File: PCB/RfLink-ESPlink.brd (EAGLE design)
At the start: 96 x 90 mm, 55 parts, among them IC1 WEMOS D1 MINI, IC2 ARDUINO-MEGA, IC3 PRO MINI 3.3V, IC4 CC2500 MODUL, IC5 TRANSMITTER 433MHZ, IC6 RXB6, IC7 RTX-MID, IC8 NRF24L01A, J2 JUMPER-3SMD, U1 AMS1117, U2 DHT22, U3 DS18B20, X1 BU-SMA-V

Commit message: Update Schema
Moved R5 closer to Mega 2560
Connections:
- net RX-TX renamed ESP-TX
- net TX-RX-L renamed ESP-RX
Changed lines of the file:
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@@
 <wire x1="93.599" y1="4.448725" x2="90.420275" y2="1.27" width="0.3048" layer="16"/>
 </signal>
-<signal name="RX-TX">
+<signal name="ESP-TX">
 <contactref element="IC1" pad="TX"/>
 <contactref element="IC3" pad="2"/>
@@
 </signal>
 <signal name="TX-RX">
+<contactref element="IC2" pad="1"/>
 <contactref element="R5" pad="2"/>
-<contactref element="IC2" pad="1"/>
-<wire x1="54.61" y1="43.18" x2="47.94" y2="43.18" width="0.3048" layer="1"/>
+<wire x1="47.94" y1="43.18" x2="54.61" y2="43.18" width="0.3048" layer="1"/>
 </signal>
-<signal name="TX-RX-L">
-<contactref element="R5" pad="1"/>
+<signal name="ESP-RX">
 <contactref element="IC1" pad="RX"/>
 <contactref element="IC3" pad="1"/>
@@
 <wire x1="43.18" y1="29.21" x2="43.18" y2="43.18" width="0.3048" layer="16"/>
 <via x="43.18" y="43.18" extent="1-16" drill="0.6"/>
-<wire x1="43.18" y1="43.18" x2="46.04" y2="43.18" width="0.3048" layer="1"/>
 <wire x1="56.1975" y1="82.2325" x2="58.42" y2="84.455" width="0.3048" layer="1"/>
 <wire x1="58.42" y1="84.455" x2="62.5475" y2="84.455" width="0.3048" layer="1"/>
@@
 <wire x1="55.41581875" y1="72.15430625" x2="53.686325" y2="73.8838" width="0.3048" layer="1"/>
 <wire x1="56.1975" y1="74.5188" x2="56.1975" y2="82.2325" width="0.3048" layer="1"/>
+<contactref element="R5" pad="1"/>
+<wire x1="43.18" y1="43.18" x2="46.04" y2="43.18" width="0.3048" layer="1"/>
 </signal>
 <signal name="N$14">

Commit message: New pcb revison 0.81
Added resistors to all Arduino Mega 2560 pins connected to ESP, value
470R. Added JP5 for external power supplt if Mega not are in use.
Unnecessary pins removed from Mega 2560.
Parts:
- removed R26: 4k7, kb20:R0805
- added JP5: (no value), kb20:GS015S-3.81-2
- added R10, R11: 1K, kb20:R0805
- IC2: value ARDUINO-MEGA -> ARDUINO MEGA 2560; device SparkFun:ARDUINO_MEGA-MIRROR -> SparkFun:ARDUINO_MEGA_MINI
- R1, R2, R3, R4, R5, R6: value 1K -> 470R
- R7: value 1k -> 470R
- R9: value 1K -> 1k
- moved R1 95.8 mm to (11.7, 16.5)
- moved R21 67.6 mm to (27.9, 68.6)
- moved R6 55.4 mm to (84.0, 76.7), turned to 0 degrees
- moved R7 50.7 mm to (84.0, 74.0)
- moved R20 50.4 mm to (84.1, 84.5), turned to 0 degrees
- moved R3 48.2 mm to (47.0, 43.2)
- moved R2 47.3 mm to (47.0, 47.3), turned to 180 degrees
- moved R5 46.5 mm to (84.0, 71.2)
- moved R9 33.8 mm to (47.0, 39.4), turned to 0 degrees
- moved R8 29.6 mm to (47.0, 35.6), turned to 180 degrees
- moved LED2 13.3 mm to (81.9, 33.0)
- moved R25 11.5 mm to (26.7, 43.2), turned to 0 degrees
- moved LED3 11.4 mm to (69.2, 33.0)
- moved R4 8.19 mm to (84.0, 79.4)
- moved R23 6.35 mm to (27.9, 58.4)
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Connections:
- removed net GPIO12: IC1.D6, IC2.RESET, IC3.22
- removed net TX-RX: IC2.1, R5.2
- new net GPIO12-RESET: IC1.D6, IC3.22, R1.2
- new net MEGA-RX: IC2.0, R2.1
- new net MEGA-TX: IC2.1, R3.2
- new net RESET: IC2.RESET, R1.1
- net +3V3: now also R21.2, R23.2, R9.2; no longer R22.2, R24.2, R7.2
- net A0: now also R25.2; no longer R26.2
- net D3-GPIO0: no longer R21.2
- net ESP-RX: now also R3.1; no longer R5.1
- net ESP-TX: now also R2.2; no longer IC2.0
- net GND: now also JP5.2, R22.1, R24.1, R8.1; no longer R21.1, R23.1, R26.1, R6.1
- net GPIO13-D7: now also R21.1, R22.2; no longer R22.1, R23.2
- net GPIO14-D5: now also R23.1, R24.2; no longer R24.1, R25.2
- net MEGA5V: now also JP5.1
- net N$1: now also R4.1; no longer R1.1
- net N$11: now also R7.2; no longer R3.2
- net N$12: now also R5.2; no longer R4.2
- net N$13: now also R4.2; no longer R1.2
- net N$16: now also R9.1; no longer R7.1
- net N$17: now also R10.1; no longer R8.1
- net N$18: now also R8.2; no longer R6.2
- net N$19: now also R11.2; no longer R9.2
- net N$2: now also R5.1; no longer R4.1
- net N$3: now also R6.1; no longer R2.1
- net N$4: now also R7.1; no longer R3.1
- net N$7: now also R11.1; no longer R9.1
- net N$8: now also R10.2; no longer R8.2
- net N$9: now also R6.2; no longer R2.2
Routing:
- net GPIO12: track 82.1 -> 0.00 mm
- net GPIO12-RESET: track 0.00 -> 75.2 mm
- net A0: track 98.8 -> 118.5 mm
- net D3-GPIO0: track 64.4 -> 83.8 mm
- net MEGA5V: track 219.3 -> 236.0 mm
- net +3V3: track 308.5 -> 317.5 mm, vias 3 -> 2
- net ESP-TX: track 49.7 -> 57.4 mm, vias 0 -> 1
- net MEGA-RX: track 0.00 -> 7.33 mm
- net TX-RX: track 6.67 -> 0.00 mm
- net MEGA-TX: track 0.00 -> 6.67 mm
- net RESET: track 0.00 -> 4.97 mm
- net N$17: track 17.7 -> 13.2 mm
- net N$8: track 93.2 -> 89.6 mm
- net N$16: track 118.8 -> 121.7 mm
- net GND: track 6.67 -> 8.89 mm, vias 21 -> 18
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- added copper zone on layer 1, net MEGA5V
- added copper zone on layer 1, net N$6
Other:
- board text added: "CC2500"
- board text added: "NRF24L01"
- board text added: "RFLINK-ESPLINK v0.81"
- board text removed: "RFLINK-ESPLINK v0.8"

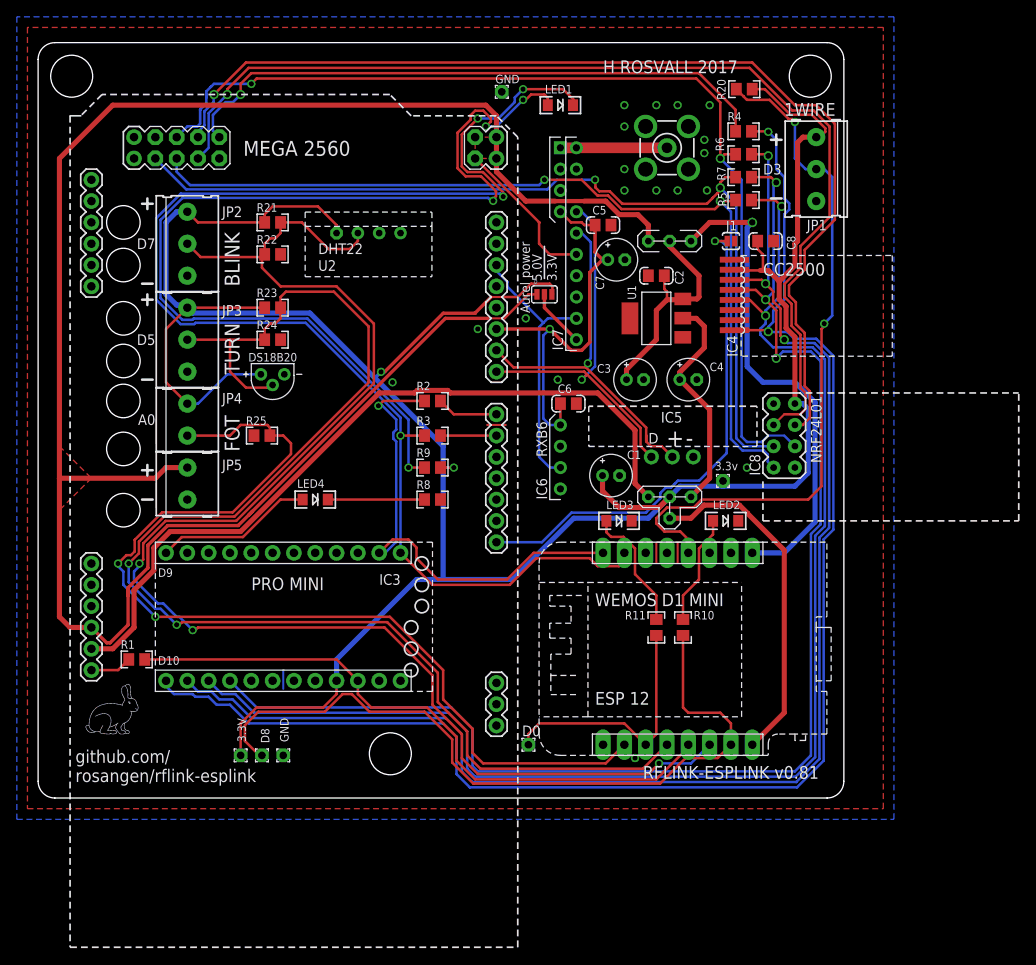
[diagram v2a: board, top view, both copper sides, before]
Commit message: New pcb revison 0.9
Added ESP-01 for easy serial debug of Wemos ESP. This is the
manufactured version. And some other good to have functions!
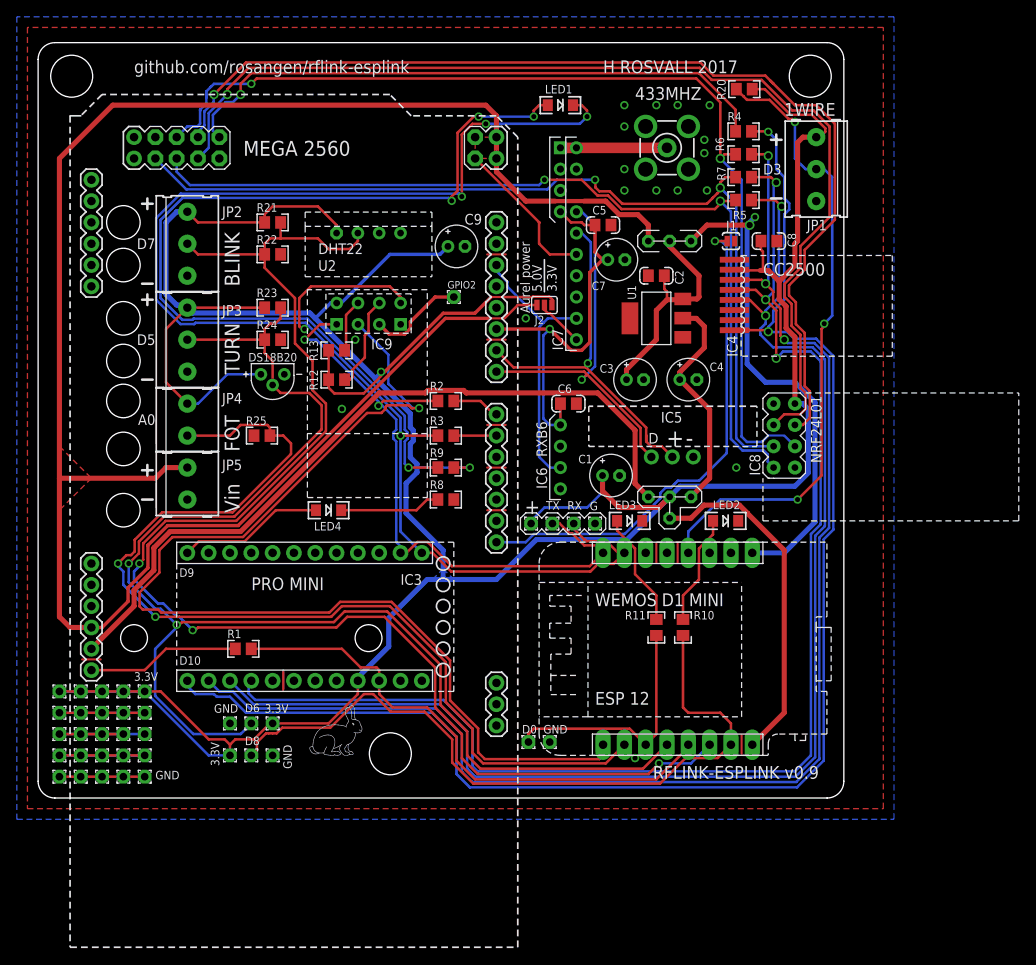
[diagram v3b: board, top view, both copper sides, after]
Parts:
- added +3.3V, P1, P10, P11, P12, P13, P14, P15, P16, P17, P18, P19, P2, P20, P21, P22, P23, P24, P25, P3, P4, P5, P6, P7, P8, P9: (no value), wirepad:1,6/0,9
- added C9: 10μF, rcl:E2-5
- added D6: D6, wirepad:1,6/0,9
- added GND5, GND7: GND, wirepad:1,6/0,9
- added GPIO2: IO2, wirepad:1,6/0,9
- added IC9: ESP-01, esp8266modules:ESP01
- added R12, R13: 4k7, kb20:R0805
- added RX: RX, wirepad:1,6/0,9
- added TX: TX, wirepad:1,6/0,9
- IC4: device CC2500A:MODULE -> CC2500A:CC2500
- moved GND 77.7 mm to (61.0, 6.67)
- moved U$28 26.8 mm to (32.1, 4.76)
- moved VCC1 23.4 mm to (58.7, 32.7)
- moved R1 12.8 mm to (24.4, 17.8)
- moved VCC2 5.39 mm to (27.9, 8.89)
- moved IC3 2.54 mm to (33.0, 21.6)
- moved LED4 2.03 mm to (34.6, 34.3)
- moved R2 1.59 mm to (48.6, 47.3)
- moved R3 1.59 mm to (48.6, 43.2)
- moved R8 1.59 mm to (48.6, 35.6)
- moved R9 1.59 mm to (48.6, 39.4)
- moved D8 1.27 mm to (25.4, 5.08)
- moved J2 1.27 mm to (60.3, 58.7)
- moved G 1.27 mm to (27.9, 5.08)
- moved LED3 1.27 mm to (70.5, 33.0)
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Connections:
- new net ESP-RESET: IC1.RESET, IC9.GPIO0
- new net N$24: IC9.CH_PD, R12.1
- new net N$26: IC9.RST, R13.1
- new net N$27: GPIO2.1, IC9.GPIO2
- new net N$28: P1.1, P2.1, P3.1, P4.1, P5.1
- new net N$29: P10.1, P6.1, P7.1, P8.1, P9.1
- new net N$31: P16.1, P17.1, P18.1, P19.1, P20.1
- net +3V3: now also +3.3V.1, C9.+, IC9.VCC, P21.1, P22.1, P23.1, P24.1, P25.1, R12.2, R13.2
- net ESP-RX: now also IC9.TX, RX.1
- net ESP-TX: now also IC9.RX, TX.1
- net GND: now also C9.-, GND5.1, GND7.1, IC9.GND, P11.1, P12.1, P13.1, P14.1, P15.1
- net GPIO14-D5: now also D6.1
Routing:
- net ESP-RESET: track 0.00 -> 129.2 mm, vias 0 -> 1
- net +3V3: track 317.5 -> 413.4 mm
- net GND: track 8.89 -> 34.6 mm, vias 18 -> 17
- net N$31: track 0.00 -> 20.3 mm
- net N$29: track 0.00 -> 20.3 mm
- net ESP-TX: track 57.4 -> 77.7 mm, vias 1 -> 2
- net N$28: track 0.00 -> 17.8 mm
- net ESP-RX: track 165.2 -> 182.9 mm, vias 4 -> 5
- net RESET: track 4.97 -> 18.2 mm
- net N$24: track 0.00 -> 11.9 mm
- net N$27: track 0.00 -> 11.7 mm
- net GPIO12-RESET: track 75.2 -> 63.8 mm
- net N$16: track 121.7 -> 111.4 mm
- net D3-GPIO0: track 83.8 -> 75.6 mm, vias 2 -> 3
- net GPIO13-D7: track 175.1 -> 168.2 mm
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- added copper zone on layer 16, net +3V3
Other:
- board text added: "433MHZ"
- board text added: "G"
- board text added: "RFLINK-ESPLINK v0.9"
- board text added: "Vin"
- board text removed: "3.3v"
- board text removed: "RFLINK-ESPLINK v0.81"
- board text removed: "github.com/ rosangen/rflink-esplink"
